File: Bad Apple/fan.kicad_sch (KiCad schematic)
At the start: 8 parts, among them J10 Conn_01x04, J2 Conn_01x02, J7 Conn_01x04, J9 Conn_01x04

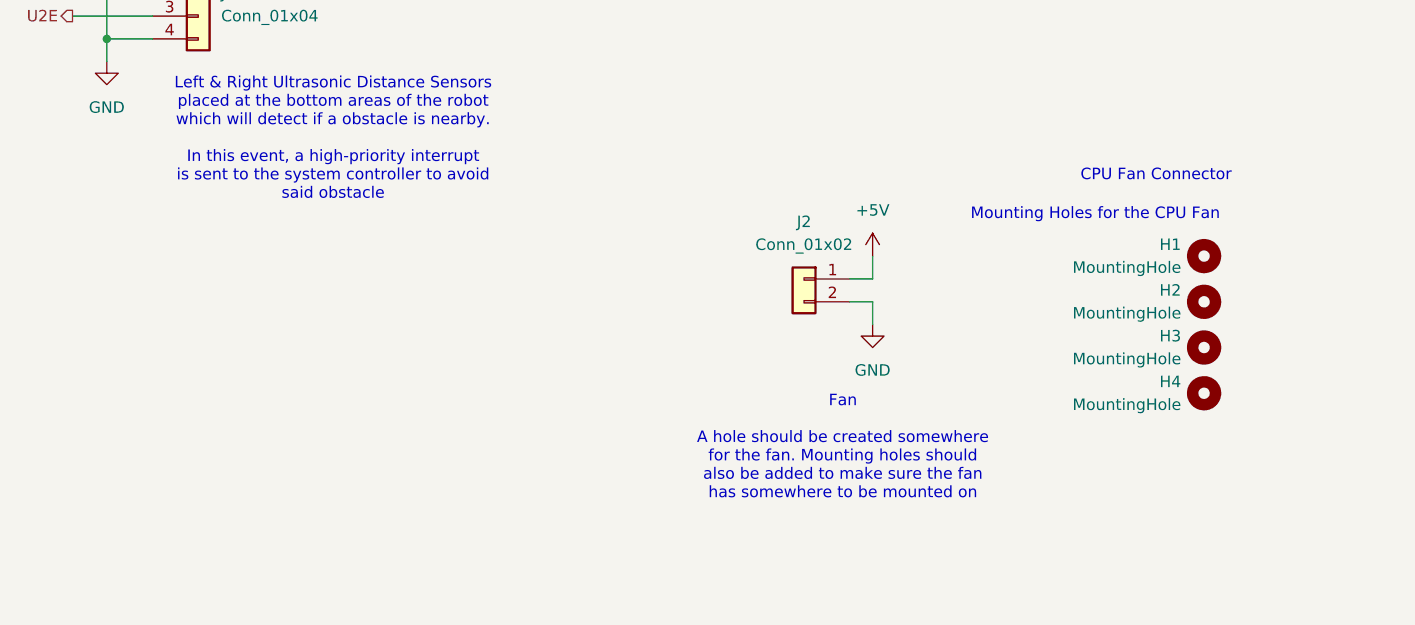
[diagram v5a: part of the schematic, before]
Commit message: feat(pcb):  connected everything to the HAT doc(pcb):  Added descriptions to the J1 pinout
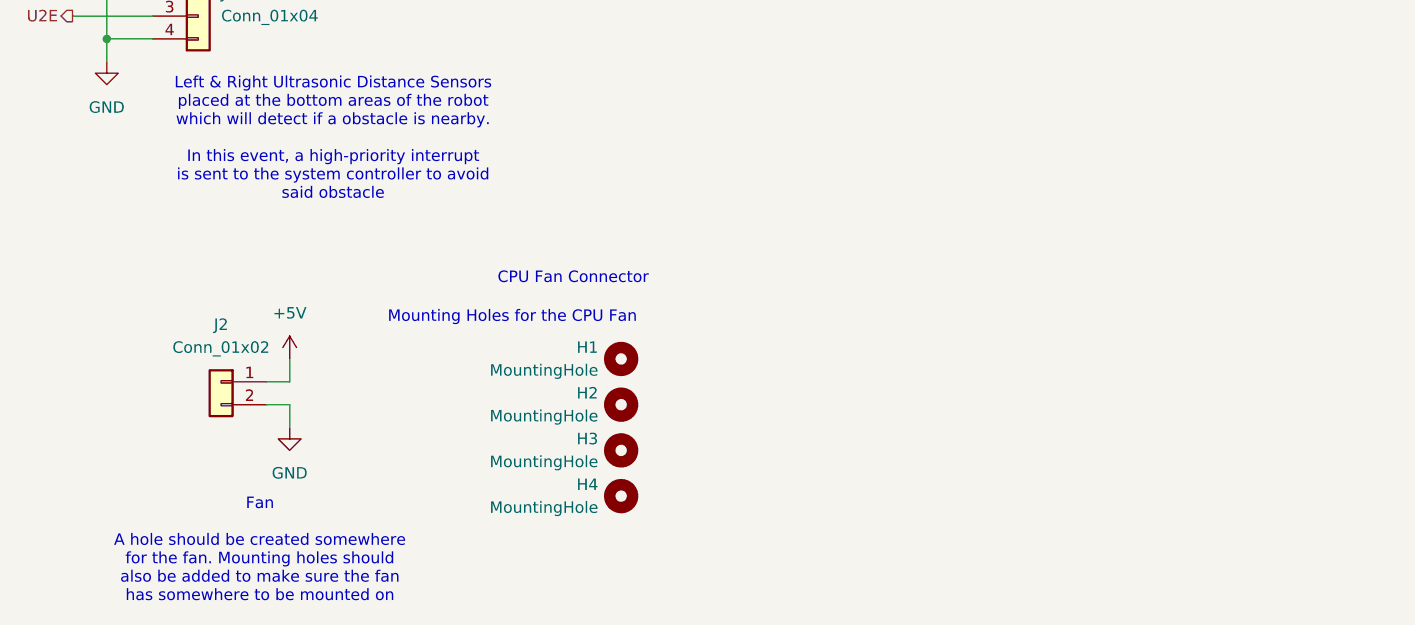
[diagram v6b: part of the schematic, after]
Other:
- moved on the sheet: H1, H2, H3, H4, J2
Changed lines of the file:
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@@
 	(text "Mounting Holes for the CPU Fan"
 		(exclude_from_sim no)
-		(at 165.608 79.248 0)
+		(at 100.838 90.678 0)
 		(effects
 			(font
@@
 	(text "Fan\n\nA hole should be created somewhere\nfor the fan. Mounting holes should\nalso be added to make sure the fan\nhas somewhere to be mounted on"
 		(exclude_from_sim no)
-		(at 123.698 105.156 0)
+		(at 58.928 116.586 0)
 		(effects
 			(font
@@
 	(text "CPU Fan Connector"
 		(exclude_from_sim no)
-		(at 158.496 74.93 0)
+		(at 93.726 86.36 0)
 		(effects
 			(font
@@
 	(wire
 		(pts
-			(xy 127 83.82) (xy 127 86.36)
-		)
-		(stroke
-			(width 0)
-			(type default)
-		)
-	)
-	(wire
-		(pts
-			(xy 127 86.36) (xy 124.46 86.36)
+			(xy 62.23 95.25) (xy 62.23 97.79)
+		)
+		(stroke
+			(width 0)
+			(type default)
+		)
+	)
+	(wire
+		(pts
+			(xy 62.23 97.79) (xy 59.69 97.79)
 		)
 		(stroke
@@
 	(wire
 		(pts
-			(xy 127 88.9) (xy 127 91.44)
+			(xy 62.23 100.33) (xy 62.23 102.87)
 		)
 		(stroke
@@
 	(wire
 		(pts
-			(xy 124.46 88.9) (xy 127 88.9)
+			(xy 59.69 100.33) (xy 62.23 100.33)
 		)
 		(stroke
@@
 		(polyline
 			(pts
-				(xy 104.14 111.76) (xy 167.64 111.76) (xy 167.64 76.2) (xy 104.14 76.2)
+				(xy 39.37 123.19) (xy 102.87 123.19) (xy 102.87 87.63) (xy 39.37 87.63)
 			)
 			(stroke
@@
 		(lib_name "+5V_1")
 		(lib_id "power:+5V")
-		(at 127 83.82 0)
+		(at 62.23 95.25 0)
 		(unit 1)
 		(exclude_from_sim no)
@@
 		(fields_autoplaced yes)
 		(property "Reference" "#PWR06"
-			(at 127 87.63 0)
+			(at 62.23 99.06 0)
 			(effects
 				(font
@@
 		)
 		(property "Value" "+5V"
-			(at 127 78.74 0)
+			(at 62.23 90.17 0)
 			(effects
 				(font
@@
 		)
 		(property "Footprint" ""
-			(at 127 83.82 0)
+			(at 62.23 95.25 0)
 			(effects
 				(font
@@
 		)
 		(property "Datasheet" ""
-			(at 127 83.82 0)
+			(at 62.23 95.25 0)
 			(effects
 				(font
@@
 		)
 		(property "Description" "Power symbol creates a global label with name \"+5V\""
-			(at 127 83.82 0)
+			(at 62.23 95.25 0)
 			(effects
 				(font
@@
 	(symbol
 		(lib_id "Mechanical:MountingHole")
-		(at 163.83 83.82 0)
+		(at 99.06 95.25 0)
 		(mirror y)
 		(unit 1)
@@
 		(fields_autoplaced yes)
 		(property "Reference" "H1"
-			(at 161.29 82.5499 0)
+			(at 96.52 93.9799 0)
 			(effects
 				(font
@@
 		)
 		(property "Value" "MountingHole"
-			(at 161.29 85.0899 0)
+			(at 96.52 96.5199 0)
 			(effects
 				(font
@@
 		)
 		(property "Footprint" "Connector_JST:JST_ACH_BM01B-ACHSS-A-GAN-ETF_1x01-1MP_P1.20mm_Vertical"
-			(at 163.83 83.82 0)
+			(at 99.06 95.25 0)
 			(effects
 				(font
@@
 		)
 		(property "Datasheet" "~"
-			(at 163.83 83.82 0)
+			(at 99.06 95.25 0)
 			(effects
 				(font
@@
 		)
 		(property "Description" "Mounting Hole without connection"
-			(at 163.83 83.82 0)
+			(at 99.06 95.25 0)
 			(effects
 				(font
@@
 	(symbol
 		(lib_id "Mechanical:MountingHole")
-		(at 163.83 88.9 0)
+		(at 99.06 100.33 0)
 		(mirror y)
 		(unit 1)
@@
 		(fields_autoplaced yes)
 		(property "Reference" "H2"
-			(at 161.29 87.6299 0)
+			(at 96.52 99.0599 0)
 			(effects
 				(font
@@
 		)
 		(property "Value" "MountingHole"
-			(at 161.29 90.1699 0)
+			(at 96.52 101.5999 0)
 			(effects
 				(font
@@
 		)
 		(property "Footprint" "Connector_JST:JST_ACH_BM01B-ACHSS-A-GAN-ETF_1x01-1MP_P1.20mm_Vertical"
-			(at 163.83 88.9 0)
+			(at 99.06 100.33 0)
 			(effects
 				(font
@@
 		)
 		(property "Datasheet" "~"
-			(at 163.83 88.9 0)
+			(at 99.06 100.33 0)
 			(effects
 				(font
@@
 		)
 		(property "Description" "Mounting Hole without connection"
-			(at 163.83 88.9 0)
+			(at 99.06 100.33 0)
 			(effects
 				(font
@@
 	(symbol
 		(lib_id "Connector_Generic:Conn_01x02")
-		(at 119.38 86.36 0)
+		(at 54.61 97.79 0)
 		(mirror y)
 		(unit 1)
@@
 		(fields_autoplaced yes)
 		(property "Reference" "J2"
-			(at 119.38 80.01 0)
+			(at 54.61 91.44 0)
 			(effects
 				(font
@@
 		)
 		(property "Value" "Conn_01x02"
-			(at 119.38 82.55 0)
+			(at 54.61 93.98 0)
 			(effects
 				(font
@@
 		)
 		(property "Footprint" "Connector_Wire:SolderWire-0.1sqmm_1x02_P3.6mm_D0.4mm_OD1mm"
-			(at 119.38 86.36 0)
+			(at 54.61 97.79 0)
 			(effects
 				(font
@@
 		)
 		(property "Datasheet" "~"
-			(at 119.38 86.36 0)
+			(at 54.61 97.79 0)
 			(effects
 				(font
@@
 		)
 		(property "Description" "Generic connector, single row, 01x02, script generated (kicad-library-utils/schlib/autogen/connector/)"
-			(at 119.38 86.36 0)
+			(at 54.61 97.79 0)
 			(effects
 				(font
@@
 	(symbol
 		(lib_id "Mechanical:MountingHole")
-		(at 163.83 93.98 0)
+		(at 99.06 105.41 0)
 		(mirror y)
 		(unit 1)
@@
 		(fields_autoplaced yes)
 		(property "Reference" "H3"
-			(at 161.29 92.7099 0)
+			(at 96.52 104.1399 0)
 			(effects
 				(font
@@
 		)
 		(property "Value" "MountingHole"
-			(at 161.29 95.2499 0)
+			(at 96.52 106.6799 0)
 			(effects
 				(font
@@
 		)
 		(property "Footprint" "Connector_JST:JST_ACH_BM01B-ACHSS-A-GAN-ETF_1x01-1MP_P1.20mm_Vertical"
-			(at 163.83 93.98 0)
+			(at 99.06 105.41 0)
 			(effects
 				(font
@@
 		)
 		(property "Datasheet" "~"
-			(at 163.83 93.98 0)
+			(at 99.06 105.41 0)
 			(effects
 				(font
@@
 		)
 		(property "Description" "Mounting Hole without connection"
-			(at 163.83 93.98 0)
+			(at 99.06 105.41 0)
 			(effects
 				(font
@@
 		(lib_name "GND_1")
 		(lib_id "power:GND")
-		(at 127 91.44 0)
+		(at 62.23 102.87 0)
 		(unit 1)
 		(exclude_from_sim no)
@@
 		(fields_autoplaced yes)
 		(property "Reference" "#PWR05"
-			(at 127 97.79 0)
+			(at 62.23 109.22 0)
 			(effects
 				(font
@@
 		)
 		(property "Value" "GND"
-			(at 127 96.52 0)
+			(at 62.23 107.95 0)
 			(effects
 				(font
@@
 		)
 		(property "Footprint" ""
-			(at 127 91.44 0)
+			(at 62.23 102.87 0)
 			(effects
 				(font
@@
 		)
 		(property "Datasheet" ""
-			(at 127 91.44 0)
+			(at 62.23 102.87 0)
 			(effects
 				(font
@@
 		)
 		(property "Description" "Power symbol creates a global label with name \"GND\" , ground"
-			(at 127 91.44 0)
+			(at 62.23 102.87 0)
 			(effects
 				(font
@@
 	(symbol
 		(lib_id "Mechanical:MountingHole")
-		(at 163.83 99.06 0)
+		(at 99.06 110.49 0)
 		(mirror y)
 		(unit 1)
@@
 		(fields_autoplaced yes)
 		(property "Reference" "H4"
-			(at 161.29 97.7899 0)
+			(at 96.52 109.2199 0)
 			(effects
 				(font
@@
 		)
 		(property "Value" "MountingHole"
-			(at 161.29 100.3299 0)
+			(at 96.52 111.7599 0)
 			(effects
 				(font
@@
 		)
 		(property "Footprint" "Connector_JST:JST_ACH_BM01B-ACHSS-A-GAN-ETF_1x01-1MP_P1.20mm_Vertical"
-			(at 163.83 99.06 0)
+			(at 99.06 110.49 0)
 			(effects
 				(font
@@
 		)
 		(property "Datasheet" "~"
-			(at 163.83 99.06 0)
+			(at 99.06 110.49 0)
 			(effects
 				(font
@@
 		)
 		(property "Description" "Mounting Hole without connection"
-			(at 163.83 99.06 0)
-			(effects
-				(font
+			(at 99.06 110.49 0)
+			(effects
+				(font
